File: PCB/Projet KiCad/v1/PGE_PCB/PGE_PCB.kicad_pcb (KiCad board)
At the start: 2 copper layers, 24 parts, among them J1 Conn_01x03_Pin, J2 GPS_Antenne, P1 USB_C_Plug_USB2.0, Q1 2N7002E, U1 STM32L476RGTx, U2 LD1117S50TR_SOT223, U3 RXM-GPS-FM, U4 LD39050PU33R, Y1 ABS25-32.768KHZ-T

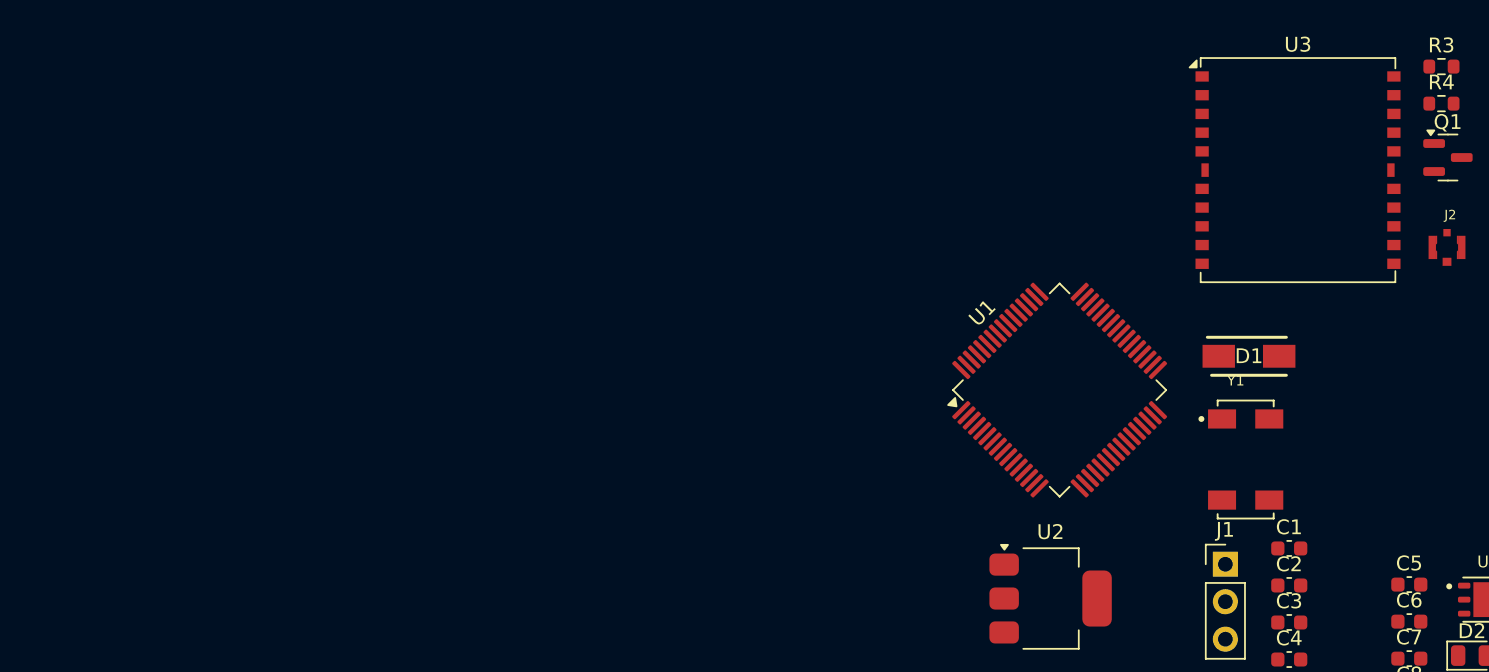
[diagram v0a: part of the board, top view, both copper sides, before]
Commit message: Maj PCB
- correction module GPS (I2C)
- ajout module LoRa RFM9x
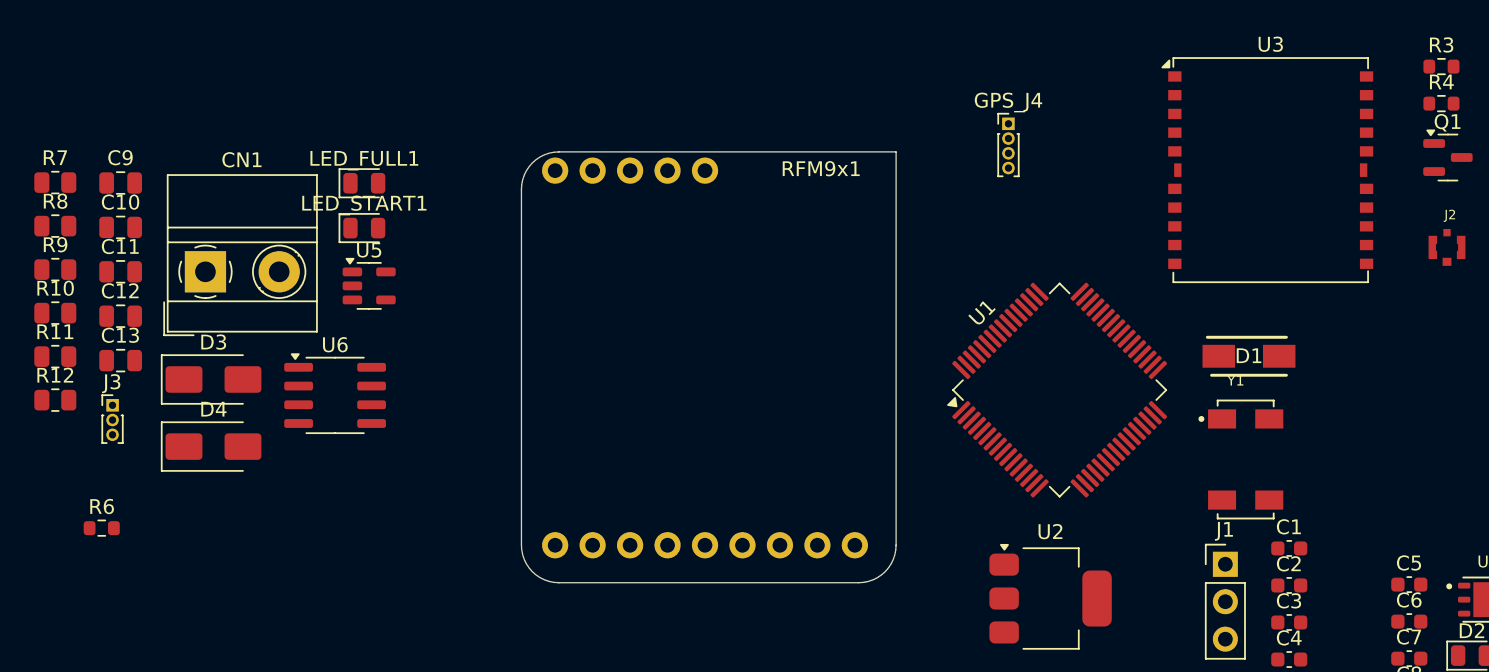
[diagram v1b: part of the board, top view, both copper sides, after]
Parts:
- added C10: 10u 16V, Capacitor_SMD:C_0805_2012Metric, F.Cu at (36.3, 45.1)
- added C11: 0.1u, Capacitor_SMD:C_0805_2012Metric, F.Cu at (36.3, 48.1)
- added C12: 100nf, Capacitor_SMD:C_0805_2012Metric, F.Cu at (36.3, 51.1)
- added C13: 0.1µf, Capacitor_SMD:C_0805_2012Metric, F.Cu at (36.3, 54.2)
- added C9: 10u 16V, Capacitor_SMD:C_0805_2012Metric, F.Cu at (36.3, 42.1)
- added CN1: Conn_01x02, TerminalBlock_MetzConnect:TerminalBlock_MetzConnect_Type011_RT05502HBWC_1x02_P5.00mm_Horizontal, F.Cu at (42.1, 48.1)
- added D3: 1N4007, Diode_SMD:D_SMA, F.Cu at (42.6, 55.4)
- added D4: 1N4007, Diode_SMD:D_SMA, F.Cu at (42.6, 60.0)
- added GPS_J4: Conn_01x04_Pin, Connector_PinHeader_1.00mm:PinHeader_1x04_P1.00mm_Vertical, F.Cu at (96.5, 38.1)
- added J3: Conn_01x03, Connector_PinHeader_1.00mm:PinHeader_1x03_P1.00mm_Vertical, F.Cu at (35.8, 57.2)
- added LED_FULL1: LED-0805_G, LED_SMD:LED_0805_2012Metric, F.Cu at (52.8, 42.1)
- added LED_START1: LED-0603_B, LED_SMD:LED_0805_2012Metric, F.Cu at (52.8, 45.2)
- added R10: 5m/1w, Resistor_SMD:R_0805_2012Metric, F.Cu at (31.9, 50.9)
- added R11: 100k, Resistor_SMD:R_0805_2012Metric, F.Cu at (31.9, 53.9)
- added R12: 4.7k, Resistor_SMD:R_0805_2012Metric, F.Cu at (31.9, 56.8)
- added R6: 4.7k, Resistor_SMD:R_0603_1608Metric, F.Cu at (35.0, 65.5)
- added R7: 470, Resistor_SMD:R_0805_2012Metric, F.Cu at (31.9, 42.1)
- added R8: 470, Resistor_SMD:R_0805_2012Metric, F.Cu at (31.9, 45.0)
- added R9: 3.9K, Resistor_SMD:R_0805_2012Metric, F.Cu at (31.9, 48.0)
- added RFM9x1: ~, LoRa_Breakout:LoRa_Breakout, F.Cu at (76.2, 53.3)
- added U5: MCP73831T, Package_TO_SOT_SMD:SOT-23-5, F.Cu at (53.2, 49.1)
- added U6: DS2438AZ+, Package_SO:SOIC-8_3.9x4.9mm_P1.27mm, F.Cu at (50.9, 56.5)
- moved U3 1.85 mm to (114.3, 41.2)
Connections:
- J1 pad 1: unconnected-(J1-Pin_1-Pad1) -> Net-(J1-Pin_1)
- P1 pad B5: unconnected-(P1-VCONN-PadB5) -> USB_5V
- U1 pad 27: unconnected-(U1-PB1-Pad27) -> LoRa_RST
- U1 pad 34: unconnected-(U1-PB13-Pad34) -> LORA_G0
- U1 pad 41: unconnected-(U1-PA8-Pad41) -> LoRa_CS
- U1 pad 42: GPS_RX -> unconnected-(U1-PA9-Pad42)
- U1 pad 43: GPS_TX -> unconnected-(U1-PA10-Pad43)
- U1 pad 55: unconnected-(U1-PB3-Pad55) -> LoRa_SCK
- U1 pad 56: unconnected-(U1-PB4-Pad56) -> LoRa_MISO
- U1 pad 57: unconnected-(U1-PB5-Pad57) -> LoRa_MOSI
- U1 pad 61: unconnected-(U1-PB8-Pad61) -> GPS_SCL
- U1 pad 62: unconnected-(U1-PB9-Pad62) -> GPS_SDA
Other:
- board outline added: 25.4 x 29.2 mm

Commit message: mise à jour Kicad
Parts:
- removed J2: GPS_Antenne, 20449-001E-03:IPEX_20449-001E-03
- removed Q1: 2N7002E, Package_TO_SOT_SMD:SOT-23
- added C14: 100nF, Capacitor_SMD:C_0805_2012Metric, F.Cu at (142.7, 23.6)
- added C15: 100nF, Capacitor_SMD:C_0805_2012Metric, F.Cu at (142.7, 26.6)
- added C16: 100nF, Capacitor_SMD:C_0805_2012Metric, F.Cu at (142.7, 29.6)
- added C17: 4.7uF, Capacitor_SMD:C_0805_2012Metric, F.Cu at (142.7, 32.7)
- added C18: 1uF, Capacitor_SMD:C_0805_2012Metric, F.Cu at (142.7, 35.7)
- added C19: 100nF, Capacitor_SMD:C_0805_2012Metric, F.Cu at (142.7, 38.7)
- added C20: 1uF, Capacitor_SMD:C_0805_2012Metric, F.Cu at (147.1, 23.6)
- added C21: 10nF, Capacitor_SMD:C_0805_2012Metric, F.Cu at (147.1, 26.6)
- added C22: 0.1u, Capacitor_SMD:C_0805_2012Metric, F.Cu at (147.1, 29.6)
- added C23: 100nf, Capacitor_SMD:C_0805_2012Metric, F.Cu at (147.1, 32.7)
- added C24: 0.1µf, Capacitor_SMD:C_0805_2012Metric, F.Cu at (147.1, 35.7)
- added CN2: Conn_01x02, TerminalBlock_MetzConnect:TerminalBlock_MetzConnect_Type011_RT05502HBWC_1x02_P5.00mm_Horizontal, F.Cu at (152.9, 29.6)
- added LED_FULL2: LED-0805_G, LED_SMD:LED_0805_2012Metric, F.Cu at (158.1, 36.2)
- added LED_START2: LED-0603_B, LED_SMD:LED_0805_2012Metric, F.Cu at (158.1, 39.2)
- added R13: 50m/1w, Resistor_SMD:R_0805_2012Metric, F.Cu at (163.6, 23.6)
- added R14: 100k, Resistor_SMD:R_0805_2012Metric, F.Cu at (163.6, 26.6)
- added R15: 4.7k, Resistor_SMD:R_0805_2012Metric, F.Cu at (163.6, 29.5)
- added ST_LINK1: Conn_01x06, Connector_JST:JST_EH_B6B-EH-A_1x06_P2.50mm_Vertical, F.Cu at (144.0, 18.9)
- added SW1: SW_Push, Button_Switch_SMD:SW_SPST_CK_KMS2xxGP, F.Cu at (152.6, 37.1)
- C1, C2, C5, C6, C7, C8: footprint Capacitor_SMD:C_0603_1608Metric -> Capacitor_SMD:C_0805_2012Metric
- C3, C4: value 10uF -> 10u 16V; footprint Capacitor_SMD:C_0603_1608Metric -> Capacitor_SMD:C_0805_2012Metric
- D1: value STPS2L30A -> 1N4007; footprint STPS2L30A:DIOM5126X265N -> Diode_SMD:D_SMA
- GPS_J4: footprint Connector_PinHeader_1.00mm:PinHeader_1x04_P1.00mm_Vertical -> Connector_PinHeader_2.54mm:PinHeader_1x04_P2.54mm_Vertical
- J1: value Conn_01x03_Pin -> Conn_01x03
- R1, R2: footprint Capacitor_SMD:C_0201_0603Metric -> Resistor_SMD:R_0805_2012Metric
- R3: value 4.7k -> 470; footprint Resistor_SMD:R_0603_1608Metric -> Resistor_SMD:R_0805_2012Metric
- R4: value 47k -> 470; footprint Resistor_SMD:R_0603_1608Metric -> Resistor_SMD:R_0805_2012Metric
- R5: footprint Resistor_SMD:R_0603_1608Metric -> Resistor_SMD:R_0805_2012Metric
- R6: value 4.7k -> 3.9K; footprint Resistor_SMD:R_0603_1608Metric -> Resistor_SMD:R_0805_2012Metric
- U2: value LD1117S50TR_SOT223 -> MCP73831T; footprint Package_TO_SOT_SMD:SOT-223-3_TabPin2 -> Package_TO_SOT_SMD:SOT-23-5
- U3: value RXM-GPS-FM -> DS2438AZ+; footprint RF_GPS:Linx_RXM-GPS -> Package_SO:SOIC-8_3.9x4.9mm_P1.27mm
- U4: footprint LD39050PU33R:SON95P300X300X100-7N -> Package_DFN_QFN:DFN-6-1EP_3x3mm_P0.95mm_EP1.7x2.6mm
- Y1: footprint ABS25-32.768KHZ-T:XTAL_ABS25-32.768KHZ-6-1-T -> Oscillator:XTAL_ABS25-32.768KHZ-6-1-T
- moved R3 7.94 mm to (118.4, 31.5)
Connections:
- C1 pad 1: GND -> VREF-
- C2 pad 1: GND -> VREF-
- C3 pad 1: VIN -> VREF-
- C3 pad 2: GND -> V+_bat_5V
- C4 pad 1: Net-(U2-VO) -> VREF-
- C4 pad 2: GND -> Net-(U2-VDD)
- C5 pad 1: ALIM -> USB_5V
- C5 pad 2: GND -> VREF-
- C6 pad 1: ALIM -> USB_5V
- C6 pad 2: GND -> VREF-
- C7 pad 1: +3.3V -> VDD
- C7 pad 2: GND -> VREF-
- C8 pad 1: +3.3V -> VDD
- C8 pad 2: GND -> VREF-
- D1 pad 1: Net-(J1-Pin_3) -> USB_5V
- D1 pad 2: Net-(U2-VO) -> V+_bat_5V
- D2 pad 1: GND -> VREF-
- GPS_J4 pad 3: GND -> VREF-
- J1 pad 1: Net-(J1-Pin_1) -> USB_5V
- J1 pad 2: ALIM -> V-_bat_5V
- J1 pad 3: Net-(J1-Pin_3) -> OneWire
- P1 pad A1: GND -> VREF-
- P1 pad A12: GND -> VREF-
- P1 pad A4: Net-(P1-VBUS-PadA4) -> USB_5V
- P1 pad A9: Net-(P1-VBUS-PadA4) -> USB_5V
- P1 pad B1: GND -> VREF-
- P1 pad B12: GND -> VREF-
- P1 pad B4: Net-(P1-VBUS-PadA4) -> USB_5V
- P1 pad B5: USB_5V -> unconnected-(P1-VCONN-PadB5)
- P1 pad B9: Net-(P1-VBUS-PadA4) -> USB_5V
- P1 pad S1: GND -> VREF-
- R3 pad 1: RESET_GPS -> Net-(LED_FULL2-Pad2)
- R3 pad 2: Net-(Q1-G) -> VREF-
- R4 pad 1: Net-(Q1-G) -> Net-(LED_START2-Pad1)
- R4 pad 2: GND -> USB_5V
- R5 pad 2: ALIM -> USB_5V
- R6 pad 1: Net-(Q2-Pad4) -> VREF-
- R6 pad 2: USB_5V -> Net-(U2-PROG)
- RFM9x1 pad 1: +3.3V -> VDD
- RFM9x1 pad 2: GND -> VREF-
- U1 pad 12: unconnected-(U1-VSSA-Pad12) -> VREF-
- U1 pad 13: unconnected-(U1-VDDA-Pad13) -> VDD
- U1 pad 17: unconnected-(U1-PA3-Pad17) -> SWO
- U1 pad 18: Net-(U1-VSS-Pad18) -> VREF-
- U1 pad 19: unconnected-(U1-VDD-Pad19) -> VDD
- U1 pad 31: Net-(U1-VSS-Pad18) -> VREF-
- U1 pad 32: unconnected-(U1-VDD-Pad32) -> VDD
- U1 pad 46: unconnected-(U1-PA13-Pad46) -> SWDIO
- U1 pad 47: Net-(U1-VSS-Pad18) -> VREF-
- U1 pad 49: unconnected-(U1-PA14-Pad49) -> SWCLK
- U1 pad 63: Net-(U1-VSS-Pad18) -> VREF-
- U1 pad 64: unconnected-(U1-VDD-Pad64) -> VDD
- U1 pad 7: unconnected-(U1-NRST-Pad7) -> NSRT
- U2 pad 1: GND -> Net-(U2-STAT)
- U2 pad 2: Net-(U2-VO) -> VREF-
- U2 pad 3: VIN -> V+_bat_5V
- U3 pad 1: unconnected-(U3-NC-Pad1) -> VREF-
- U3 pad 2: unconnected-(U3-NC-Pad2) -> V-_bat_5V
- U3 pad 3: unconnected-(U3-1PPS-Pad3) -> Net-(U3-VSENS-)
- U3 pad 4: GPS_TX -> V+_bat_5V
- U3 pad 5: GPS_RX -> V+_bat_5V
- U3 pad 8: Net-(Q1-S) -> OneWire
- U4 pad 1: ALIM -> USB_5V
- U4 pad 2: GND -> VREF-
- U4 pad 4: +3.3V -> VDD
- U4 pad 6: ALIM -> USB_5V
- U4 pad 7: GND -> VREF-

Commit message: fin routage prototype_V1
Pour avis Kristen
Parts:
- removed C11: 0.1u, Capacitor_SMD:C_0805_2012Metric
- removed C12: 100nf, Capacitor_SMD:C_0805_2012Metric
- removed C13: 0.1µf, Capacitor_SMD:C_0805_2012Metric
- removed CN1: Conn_01x02, TerminalBlock_MetzConnect:TerminalBlock_MetzConnect_Type011_RT05502HBWC_1x02_P5.00mm_Horizontal
- removed D3, D4: 1N4007, Diode_SMD:D_SMA
- removed J3: Conn_01x03, Connector_PinHeader_1.00mm:PinHeader_1x03_P1.00mm_Vertical
- removed LED_FULL1: LED-0805_G, LED_SMD:LED_0805_2012Metric
- removed LED_START1: LED-0603_B, LED_SMD:LED_0805_2012Metric
- removed R10: 5m/1w, Resistor_SMD:R_0805_2012Metric
- removed R11: 100k, Resistor_SMD:R_0805_2012Metric
- removed R12: 4.7k, Resistor_SMD:R_0805_2012Metric
- removed R7, R8: 470, Resistor_SMD:R_0805_2012Metric
- removed R9: 3.9K, Resistor_SMD:R_0805_2012Metric
- removed U6: DS2438AZ+, Package_SO:SOIC-8_3.9x4.9mm_P1.27mm
- added I2C1: Conn_01x04_Pin, Connector_PinHeader_2.54mm:PinHeader_1x04_P2.54mm_Vertical, F.Cu at (102.5, 96.5)
- added SPI_SD1: Conn_01x06_Socket, Connector_PinHeader_2.54mm:PinHeader_1x06_P2.54mm_Vertical, F.Cu at (117.3, 112.0)
- added UART1: Conn_01x04_Pin, Connector_PinHeader_2.54mm:PinHeader_1x04_P2.54mm_Vertical, F.Cu at (94.7, 104.6)
- C10: value 10u 16V -> 4.7uF; moved to B.Cu
- C14, C15, C16, C17, C22, C23, C24, C3, C4, C5, C6, C7, C8, D1, D2, LED_FULL2, LED_START2, R13, R14, R15, R3, R4, R5, R6, U2, U3, U4: moved to B.Cu
- C9: value 10u 16V -> 0.1uF; moved to B.Cu
- U5: value MCP73831T -> SiP32431DR3; footprint Package_TO_SOT_SMD:SOT-23-5 -> Package_TO_SOT_SMD:SOT-363_SC-70-6; moved to B.Cu
- moved C10 116.4 mm to (140.3, 97.5), turned to 180 degrees
- moved C9 116.4 mm to (140.3, 94.5), turned to 180 degrees
- moved R6 112.1 mm to (140.0, 105.0), turned to 90 degrees
- moved ST_LINK1 101.5 mm to (122.9, 118.2)
- moved U5 94.7 mm to (135.9, 95.0), turned to 180 degrees
- moved C20 89.3 mm to (124.6, 110.0)
- moved CN2 87.8 mm to (158.5, 117.2)
- moved R3 85.9 mm to (151.0, 111.0), turned to 180 degrees
- moved C21 81.5 mm to (124.6, 105.0)
- moved P1 78.9 mm to (98.9, 119.1)
- moved RFM9x1 75.7 mm to (148.0, 77.2)
- moved C19 73.0 mm to (129.6, 110.5)
- moved SW1 72.9 mm to (114.2, 99.0), turned to -90 degrees
- moved C18 71.1 mm to (129.2, 105.5)
- moved LED_FULL2 68.9 mm to (154.0, 104.9), turned to -90 degrees
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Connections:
- C10 pad 1: GND -> VDD
- C10 pad 2: Net-(U5-VDD) -> VREF-
- C9 pad 1: GND -> VDD_LORA
- C9 pad 2: Vbat+ -> VREF-
- GPS_J4 pad 4: +3.3V -> VDD
- RFM9x1 pad 1: VDD -> VDD_LORA
- U1 pad 16: unconnected-(U1-PA2-Pad16) -> CMD_PW
- U1 pad 21: unconnected-(U1-PA5-Pad21) -> SCK_SD
- U1 pad 22: unconnected-(U1-PA6-Pad22) -> MISO_SPI
- U1 pad 23: unconnected-(U1-PA7-Pad23) -> MOSI_SD
- U1 pad 38: unconnected-(U1-PC7-Pad38) -> OneWire
- U1 pad 42: unconnected-(U1-PA9-Pad42) -> Tx_uart
- U1 pad 43: unconnected-(U1-PA10-Pad43) -> Rx_uart
- U1 pad 58: unconnected-(U1-PB6-Pad58) -> CS_SD
- U1 pad 8: unconnected-(U1-PC0-Pad8) -> SCL
- U1 pad 9: unconnected-(U1-PC1-Pad9) -> SDA
- U5 pad 1: Net-(U5-STAT) -> VDD_LORA
- U5 pad 2: GND -> VREF-
- U5 pad 3: Vbat+ -> CMD_PW
- U5 pad 4: Net-(U5-VDD) -> VDD
- U5 pad 5: Net-(U5-PROG) -> VREF-
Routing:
- net VREF-: track 0.00 -> 361.3 mm, vias 0 -> 9
- net VDD: track 0.00 -> 146.8 mm, vias 0 -> 6
- net USB_5V: track 0.00 -> 109.6 mm, vias 0 -> 4
- net V+_bat_5V: track 0.00 -> 99.0 mm, vias 0 -> 1
- net Rx_uart: track 0.00 -> 64.3 mm, vias 0 -> 2
- net SWDIO: track 0.00 -> 63.9 mm, vias 0 -> 1
- net OneWire: track 0.00 -> 60.5 mm, vias 0 -> 1
- net Tx_uart: track 0.00 -> 55.1 mm, vias 0 -> 2
- net V-_bat_5V: track 0.00 -> 50.8 mm, vias 0 -> 1
- net SWCLK: track 0.00 -> 50.1 mm, vias 0 -> 1
- net NSRT: track 0.00 -> 47.8 mm, vias 0 -> 2
- net CS_SD: track 0.00 -> 40.1 mm, vias 0 -> 1
- net LoRa_MOSI: track 0.00 -> 38.7 mm, vias 0 -> 1
- net LoRa_SCK: track 0.00 -> 36.3 mm, vias 0 -> 1
- net LoRa_RST: track 0.00 -> 33.5 mm
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- added copper zone on B.Cu, net VREF-
- added copper zone on F.Cu, net VREF-
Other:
- board size 25.4 x 29.2 mm -> 77 x 61.5 mm

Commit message: PCB_Proto_PGE  Terminé
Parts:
- C10, C3, C4, C5, C6, C9, LED_FULL2, LED_START2, R3, R4, R6, U2, U4, U5: moved to F.Cu
- C18, C19, C20, C21: moved to B.Cu
- moved C24 29.7 mm to (143.8, 100.6)
- moved C9 28.9 mm to (132.8, 66.5)
- moved C10 25.5 mm to (132.8, 73.2), turned to 0 degrees
- moved U5 25.3 mm to (132.8, 69.8), turned to -90 degrees
- moved R14 24.5 mm to (152.1, 99.8), turned to -90 degrees
- moved C18 23.1 mm to (115.5, 86.8), turned to -90 degrees
- moved C19 21.7 mm to (116.8, 93.0), turned to 180 degrees
- moved C20 21.3 mm to (116.8, 90.2), turned to 180 degrees
- moved ST_LINK1 19.5 mm to (142.0, 121.9), turned to 180 degrees
- moved C21 19.5 mm to (117.7, 86.8), turned to 90 degrees
- moved R15 16.5 mm to (140.0, 94.0)
- moved U3 16.0 mm to (145.8, 94.0)
- moved R4 15.8 mm to (135.6, 110.0), turned to 180 degrees
- moved C23 15.7 mm to (148.3, 100.6), turned to 0 degrees
- moved U4 13.8 mm to (133.5, 114.6), turned to 0 degrees
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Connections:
- C19 pad 1: VREF -> VDD
- C20 pad 1: VREF+ -> VDD
- U1 pad 35: unconnected-(U1-PB14-Pad35) -> LORA_G1
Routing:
- net VREF-: track 361.3 -> 0.00 mm, vias 9 -> 4
- net LORA_G1: track 0.00 -> 58.1 mm, vias 0 -> 2
- net VDD: track 146.8 -> 196.4 mm, vias 6 -> 2
- net V+_bat_5V: track 99.0 -> 62.5 mm, vias 1 -> 0
- net LoRa_MOSI: track 38.7 -> 14.2 mm, vias 1 -> 0
- net Rx_uart: track 64.3 -> 42.0 mm
- net SWDIO: track 63.9 -> 42.5 mm
- net CMD_PW: track 16.6 -> 37.4 mm, vias 1 -> 2
- net OneWire: track 60.5 -> 40.4 mm
- net LoRa_SCK: track 36.3 -> 16.6 mm
- net LoRa_CS: track 32.9 -> 13.7 mm
- net SCL: track 21.1 -> 38.7 mm, vias 0 -> 1
- net SDA: track 22.0 -> 36.2 mm, vias 0 -> 1
- net Net-(U3-VSENS-): track 20.9 -> 7.69 mm
- net Net-(LED_START2-Pad1): track 7.42 -> 19.6 mm
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
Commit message: Update PCB
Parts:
- moved C14 0.12 mm to (118.5, 75.4)
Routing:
- net CMD_PW: track 37.4 -> 31.1 mm
- net SCL: track 38.7 -> 35.1 mm
- net LORA_G1: track 58.1 -> 60.2 mm, vias 2 -> 1
- net VDD: track 196.4 -> 198.1 mm
- net GPS_SDA: track 34.8 -> 36.3 mm
- net GPS_SCL: track 34.4 -> 35.8 mm
- net LoRa_MOSI: track 14.2 -> 15.6 mm
- net SWO: track 34.0 -> 35.3 mm
- net Net-(LED_FULL2-Pad2): track 16.8 -> 15.6 mm
- net Net-(LED_START2-Pad1): track 19.6 -> 20.5 mm
- net Net-(C2-Pad2): track 8.98 -> 8.24 mm
- net Net-(C14-Pad2): track 14.0 -> 14.7 mm
- net LoRa_CS: track 13.7 -> 13.1 mm
- net USB_5V: track 112.8 -> 112.2 mm
- net LoRa_RST: track 22.4 -> 22.9 mm
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
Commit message: Pcb VERSION GPS séparer
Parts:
- removed GPS_J4: Conn_01x04_Pin, Connector_PinHeader_2.54mm:PinHeader_1x04_P2.54mm_Vertical
- removed U4: LD39050PU33R, Package_DFN_QFN:DFN-6-1EP_3x3mm_P0.95mm_EP1.7x2.6mm
- added GPS_J4_I2C1: Conn_01x04_Pin, Connector_PinHeader_2.54mm:PinHeader_1x04_P2.54mm_Vertical, F.Cu at (138.0, 46.0)
- added SPI_SD2: Conn_01x06_Socket, Connector_PinHeader_2.54mm:PinHeader_1x06_P2.54mm_Vertical, F.Cu at (122.0, 68.7)
- added U6: LD1117S33TR_SOT223, Package_TO_SOT_SMD:SOT-223-3_TabPin2, B.Cu at (132.0, 88.0)
- C10, C3, C4, C5, C6, C9, LED_FULL2, LED_START2, R3, R4, R6, U2, U5: moved to B.Cu
- C22, C23, C24, D1, R13, R14, R15, U3: moved to F.Cu
- P1: footprint Connector_USB:USB_C_Plug_Molex_105444 -> Connector_USB:USB_C_Receptacle_Palconn_UTC16-G
- moved ST_LINK1 81.2 mm to (165.0, 44.0)
- moved UART1 58.6 mm to (155.0, 96.0), turned to 90 degrees
- moved R4 58.5 mm to (191.0, 91.0), turned to 0 degrees
- moved R15 48.3 mm to (185.5, 77.9)
- moved I2C1 47.8 mm to (138.0, 81.0), turned to 90 degrees
- moved R3 46.1 mm to (185.0, 97.0)
- moved C19 44.0 mm to (147.0, 61.0), turned to 90 degrees
- moved C18 43.9 mm to (151.0, 61.0), turned to 90 degrees
- moved C3 43.8 mm to (180.0, 97.0), turned to 180 degrees
- moved J1 43.5 mm to (197.0, 71.0)
- moved D1 43.2 mm to (188.0, 71.0), turned to 180 degrees
- moved C14 42.1 mm to (160.0, 83.0), turned to 90 degrees
- moved P1 41.3 mm to (135.0, 99.0)
- moved RFM9x1 39.1 mm to (184.0, 52.7), turned to 90 degrees
- moved U2 38.7 mm to (176.0, 93.0), turned to 180 degrees
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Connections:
- U1 pad 14: unconnected-(U1-PA0-Pad14) -> standby
- U1 pad 15: unconnected-(U1-PA1-Pad15) -> GPS_reset
- U1 pad 29: unconnected-(U1-PB10-Pad29) -> Tx_uart
- U1 pad 30: unconnected-(U1-PB11-Pad30) -> Rx_uart
- U1 pad 42: Tx_uart -> GPS_RX
- U1 pad 43: Rx_uart -> GPS_TX
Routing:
- net VREF-: track 0.00 -> 348.6 mm, vias 3 -> 9
- net GPS_RX: track 0.00 -> 54.8 mm, vias 0 -> 2
- net LoRa_RST: track 22.9 -> 73.7 mm, vias 1 -> 3
- net LORA_G0: track 21.8 -> 69.7 mm
- net LoRa_CS: track 13.1 -> 60.3 mm, vias 0 -> 2
- net GPS_TX: track 0.00 -> 44.9 mm
- net GPS_reset: track 0.00 -> 41.8 mm, vias 0 -> 1
- net LORA_G1: track 60.2 -> 19.3 mm
- net LoRa_MOSI: track 15.6 -> 56.0 mm, vias 0 -> 1
- net standby: track 0.00 -> 39.8 mm
- net VDD_LORA: track 8.77 -> 40.7 mm, vias 0 -> 2
- net LoRa_MISO: track 17.5 -> 49.1 mm, vias 1 -> 0
- net LoRa_SCK: track 16.6 -> 47.5 mm, vias 1 -> 0
- net Tx_uart: track 48.5 -> 17.7 mm, vias 2 -> 1
- net Rx_uart: track 42.0 -> 16.8 mm, vias 2 -> 1
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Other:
- board size 77 x 61.5 mm -> 85.5 x 66.8 mm
